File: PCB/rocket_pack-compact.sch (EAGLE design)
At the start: 22 parts, among them Q2 QUARZ5, U1 TPS73632_DBV_5, U2 LTC1540, U3 MSP430FR5739_DA_38

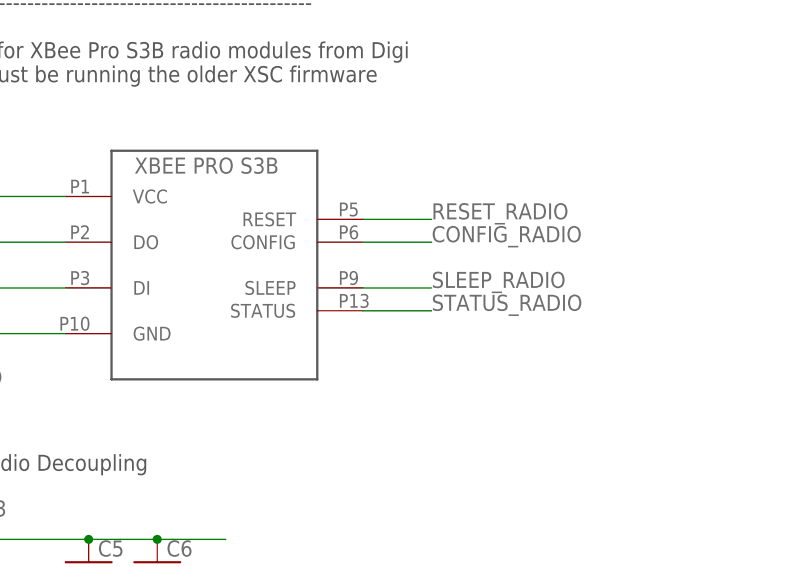
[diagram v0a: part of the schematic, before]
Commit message: firmware + PCB update
Start of main firmware..mainly UART code
Update to PCB to move "command" line from radio pin 6 to 16.  Pin 6
enters command mode on boot, pin 16 enables binary command mode
(allowing the serial +++ handshake to be bypassed
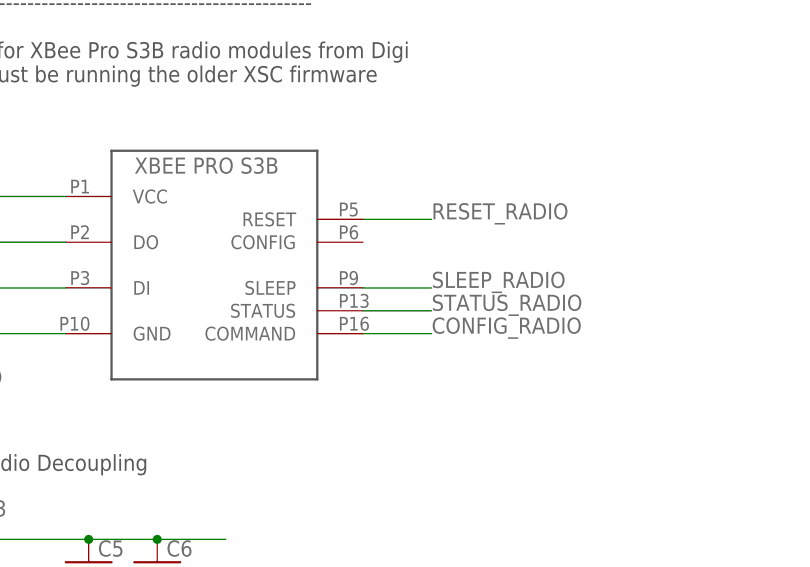
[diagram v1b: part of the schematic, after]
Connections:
- net CONFIG_RADIO: now also U$1.COMMAND; no longer U$1.CONFIG
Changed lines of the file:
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@@
 <net name="CONFIG_RADIO" class="0">
-<segment>
-<pinref part="U$1" gate="G$1" pin="CONFIG"/>
-<wire x1="48.26" y1="30.48" x2="55.88" y2="30.48" width="0.1524" layer="91"/>
-<label x="55.88" y="30.48" size="1.778" layer="95"/>
-</segment>
 <segment>
 <pinref part="U3" gate="A" pin="P3.6/TB2.1/TB1CLK"/>
@@
 <label x="53.34" y="-160.02" size="1.778" layer="95"/>
 </segment>
+<segment>
+<pinref part="U$1" gate="G$1" pin="COMMAND"/>
+<wire x1="48.26" y1="20.32" x2="55.88" y2="20.32" width="0.1524" layer="91"/>
+<label x="55.88" y="20.32" size="1.778" layer="95"/>
+</segment>
 </net>

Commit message: Version 0.2
Moved programming header to no longer interfere with headers
Fixed pinout on radio module to allow binary programming
Added power indicator LED
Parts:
- added LED1: 2V, adafruit:LEDSMT1206
- added R4: 100, adafruit:R-US_R1206
- C7, C8: value 12p -> 23p
- R2: value 5.1M -> 2M
- R3: value 3M -> 1.18M
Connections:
- new net LED: LED1.C, R4.2
- net +3V3: now also LED1.A
- net GND: now also R4.1
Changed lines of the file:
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@@
 <part name="U1" library="TexasInstruments" deviceset="TPS73632_DBV_5" device=""/>
 <part name="U2" library="linear" deviceset="LTC1540" device=""/>
-<part name="R2" library="adafruit" deviceset="R-US_" device="R1206" value="5.1M"/>
-<part name="R3" library="adafruit" deviceset="R-US_" device="R1206" value="3M"/>
+<part name="R2" library="adafruit" deviceset="R-US_" device="R1206" value="2M"/>
+<part name="R3" library="adafruit" deviceset="R-US_" device="R1206" value="1.18M"/>
 <part name="P+3" library="supply1" deviceset="VCC" device=""/>
 <part name="SUPPLY6" library="supply2" deviceset="GND" device=""/>
@@
 <part name="FRAME1" library="frames" deviceset="TABL_L" device=""/>
 <part name="JP3" library="adafruit" deviceset="PINHD-2X4" device=""/>
-<part name="C7" library="adafruit" deviceset="C-US" device="C1206" value="12p"/>
-<part name="C8" library="adafruit" deviceset="C-US" device="C1206" value="12p"/>
+<part name="C7" library="adafruit" deviceset="C-US" device="C1206" value="23p"/>
+<part name="C8" library="adafruit" deviceset="C-US" device="C1206" value="23p"/>
+<part name="LED1" library="adafruit" deviceset="LED" device="SMT1206" value="2V"/>
+<part name="R4" library="adafruit" deviceset="R-US_" device="R1206" value="100"/>
+<part name="SUPPLY12" library="supply2" deviceset="GND" device=""/>
+<part name="+3V6" library="supply1" deviceset="+3V3" device=""/>
 </parts>
 <sheets>
@@
 <instance part="C7" gate="G$1" x="63.5" y="-86.36" rot="R90"/>
 <instance part="C8" gate="G$1" x="63.5" y="-111.76" rot="R90"/>
+<instance part="LED1" gate="G$1" x="-38.1" y="-35.56" rot="R90"/>
+<instance part="R4" gate="G$1" x="-22.86" y="-35.56" rot="R180"/>
+<instance part="SUPPLY12" gate="GND" x="-12.7" y="-38.1"/>
+<instance part="+3V6" gate="G$1" x="-48.26" y="-35.56" rot="R270"/>
 </instances>
 <busses>
@@
 <label x="218.44" y="-45.72" size="1.778" layer="95"/>
 </segment>
+<segment>
+<pinref part="R4" gate="G$1" pin="1"/>
+<pinref part="SUPPLY12" gate="GND" pin="GND"/>
+<wire x1="-17.78" y1="-35.56" x2="-12.7" y2="-35.56" width="0.1524" layer="91"/>
+</segment>
 </net>
 <net name="VCC" class="0">
@@
 <label x="195.58" y="-45.72" size="1.778" layer="95" rot="R180"/>
 </segment>
+<segment>
+<pinref part="LED1" gate="G$1" pin="A"/>
+<pinref part="+3V6" gate="G$1" pin="+3V3"/>
+<wire x1="-50.8" y1="-35.56" x2="-40.64" y2="-35.56" width="0.1524" layer="91"/>
+</segment>
 </net>
 <net name="RST" class="0">
@@
 </segment>
 </net>
+<net name="LED" class="0">
+<segment>
+<pinref part="LED1" gate="G$1" pin="C"/>
+<pinref part="R4" gate="G$1" pin="2"/>
+<wire x1="-33.02" y1="-35.56" x2="-27.94" y2="-35.56" width="0.1524" layer="91"/>
+</segment>
+</net>
